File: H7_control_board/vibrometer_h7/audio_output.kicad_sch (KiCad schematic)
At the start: 31 parts, among them J901 PJ-3270, U901 RC4580, U902 TPA6111A2

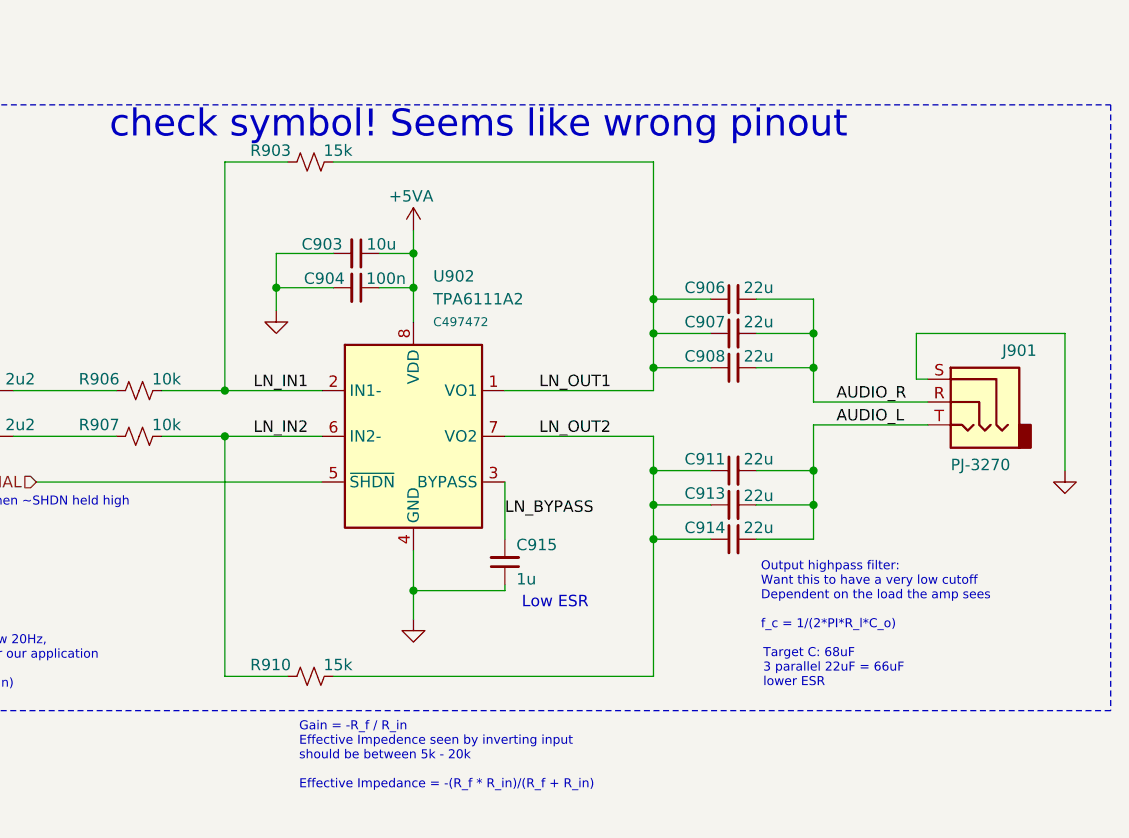
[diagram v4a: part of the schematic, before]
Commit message: cleaned up silkscreen
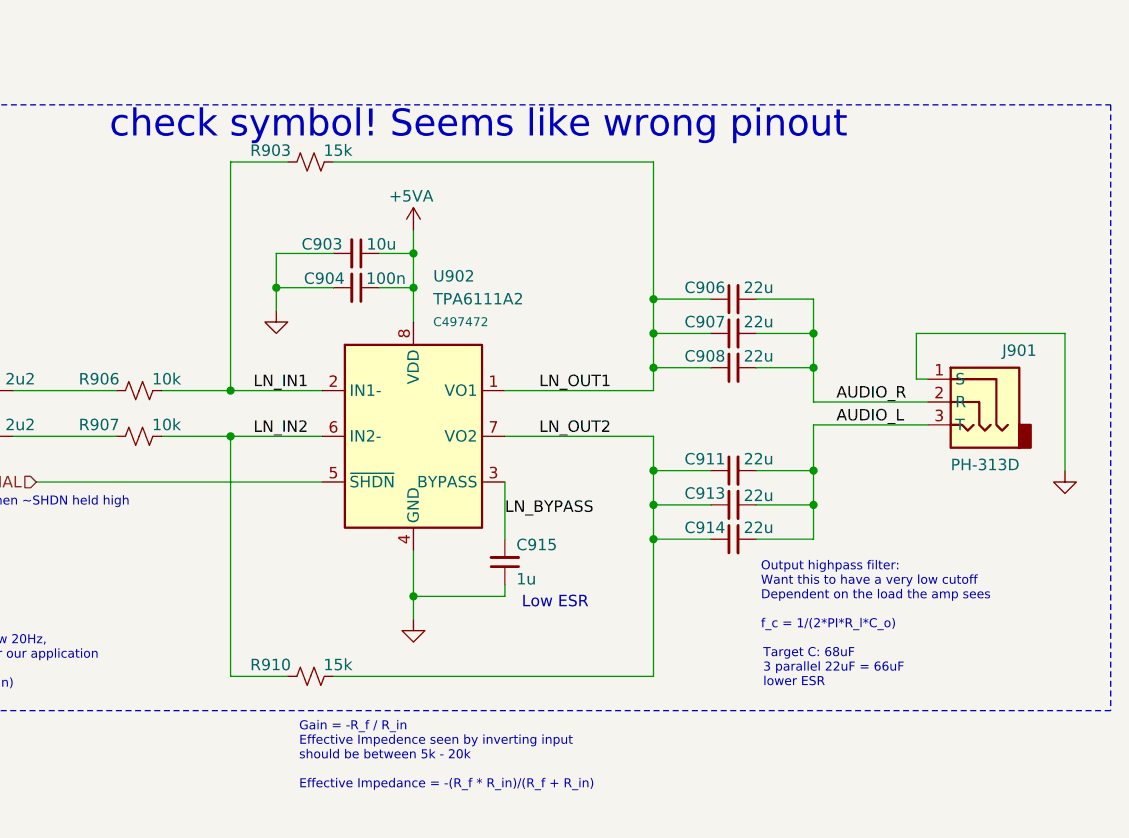
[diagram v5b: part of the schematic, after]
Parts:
- J901: value PJ-3270 -> PH-313D; footprint footprints:AUDIO-TH_PJ-3270 -> footprints:AUDIO-SMD_PJ-313D-2; LCSC C381134 -> C668608
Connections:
- net AUDIO_L: now also J901.3 (T); no longer J901.T
- net AUDIO_R: now also J901.2 (R); no longer J901.R
- net GND: now also J901.1 (S); no longer J901.S
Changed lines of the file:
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@@
 	(paper "A4")
 	(junction
-		(at 193.04 128.905)
-		(diameter 0)
-		(color 0 0 0 0)
-	)
-	(junction
 		(at 219.71 115.57)
 		(diameter 0)
@@
 	)
 	(junction
+		(at 172.72 106.68)
+		(diameter 0)
+		(color 0 0 0 0)
+	)
+	(junction
 		(at 193.04 95.25)
 		(diameter 0)
@@
 	)
 	(junction
-		(at 172.085 111.76)
-		(diameter 0)
-		(color 0 0 0 0)
-	)
-	(junction
 		(at 177.8 95.25)
 		(diameter 0)
@@
 	)
 	(junction
-		(at 172.085 106.68)
-		(diameter 0)
-		(color 0 0 0 0)
-	)
-	(junction
 		(at 66.04 152.4)
 		(diameter 0)
@@
 	)
 	(junction
+		(at 172.72 111.76)
+		(diameter 0)
+		(color 0 0 0 0)
+	)
+	(junction
 		(at 95.25 134.62)
 		(diameter 0)
@@
 	)
 	(junction
+		(at 193.04 129.54)
+		(diameter 0)
+		(color 0 0 0 0)
+	)
+	(junction
 		(at 54.61 132.08)
 		(diameter 0)
@@
 	(wire
 		(pts
-			(xy 172.085 81.28) (xy 179.07 81.28)
+			(xy 172.72 81.28) (xy 179.07 81.28)
 		)
 		(stroke
@@
 	(wire
 		(pts
-			(xy 165.1 111.76) (xy 172.085 111.76)
+			(xy 165.1 111.76) (xy 172.72 111.76)
 		)
 		(stroke
@@
 	(wire
 		(pts
-			(xy 165.1 106.68) (xy 172.085 106.68)
+			(xy 165.1 106.68) (xy 172.72 106.68)
 		)
 		(stroke
@@
 	(wire
 		(pts
-			(xy 193.04 128.905) (xy 203.2 128.905)
+			(xy 193.04 129.54) (xy 203.2 129.54)
+		)
+		(stroke
+			(width 0)
+			(type default)
+		)
+	)
+	(wire
+		(pts
+			(xy 172.72 111.76) (xy 182.88 111.76)
 		)
 		(stroke
@@
 	(wire
 		(pts
-			(xy 193.04 128.905) (xy 193.04 124.46)
+			(xy 193.04 124.46) (xy 193.04 129.54)
 		)
 		(stroke
@@
 	(wire
 		(pts
-			(xy 172.085 81.28) (xy 172.085 106.68)
+			(xy 172.72 81.28) (xy 172.72 106.68)
 		)
 		(stroke
@@
 	(wire
 		(pts
-			(xy 172.085 106.68) (xy 182.88 106.68)
-		)
-		(stroke
-			(width 0)
-			(type default)
-		)
-	)
-	(wire
-		(pts
 			(xy 74.93 69.85) (xy 54.61 69.85)
 		)
@@
 	(wire
 		(pts
+			(xy 172.72 106.68) (xy 182.88 106.68)
+		)
+		(stroke
+			(width 0)
+			(type default)
+		)
+	)
+	(wire
+		(pts
 			(xy 265.43 100.33) (xy 265.43 115.57)
 		)
@@
 	(wire
 		(pts
-			(xy 203.2 128.27) (xy 203.2 128.905)
+			(xy 203.2 128.27) (xy 203.2 129.54)
 		)
 		(stroke
@@
 	(wire
 		(pts
-			(xy 179.07 138.43) (xy 172.085 138.43)
+			(xy 179.07 138.43) (xy 172.72 138.43)
 		)
 		(stroke
@@
 	(wire
 		(pts
-			(xy 193.04 132.08) (xy 193.04 128.905)
+			(xy 193.04 132.08) (xy 193.04 129.54)
 		)
 		(stroke
@@
 	(wire
 		(pts
-			(xy 172.085 138.43) (xy 172.085 111.76)
+			(xy 172.72 138.43) (xy 172.72 111.76)
 		)
 		(stroke
@@
 		(pts
 			(xy 74.93 137.16) (xy 74.93 142.24)
-		)
-		(stroke
-			(width 0)
-			(type default)
-		)
-	)
-	(wire
-		(pts
-			(xy 172.085 111.76) (xy 182.88 111.76)
 		)
 		(stroke
@@
 			)
 		)
-		(property "Value" "PJ-3270"
+		(property "Value" "PH-313D"
 			(at 252.73 114.935 0)
 			(effects
@@
 			)
 		)
-		(property "Footprint" "footprints:AUDIO-TH_PJ-3270"
-			(at 255.27 107.95 0)
-			(effects
-				(font
-					(size 1.27 1.27)
-				)
-				(hide yes)
-			)
-		)
-		(property "Datasheet" "https://wmsc.lcsc.com/wmsc/upload/file/pdf/v2/lcsc/2110151630_XKB-Connection-PJ-3270_C381134.pdf"
-			(at 255.27 107.95 0)
+		(property "Footprint" "footprints:AUDIO-SMD_PJ-313D-2"
+			(at 255.27 95.758 0)
+			(effects
+				(font
+					(size 1.27 1.27)
+				)
+				(hide yes)
+			)
+		)
+		(property "Datasheet" "https://www.lcsc.com/datasheet/lcsc_datasheet_2006181822_SHOU-HAN-PJ-313D_C668608.pdf"
+			(at 255.27 97.79 0)
 			(effects
 				(font
@@
 		)
 		(property "Description" "Audio Jack, 3 Poles (Stereo / TRS)"
-			(at 255.27 107.95 0)
-			(effects
-				(font
-					(size 1.27 1.27)
-				)
-				(hide yes)
-			)
-		)
-		(property "LCSC" "C381134"
-			(at 255.27 107.95 0)
-			(effects
-				(font
-					(size 1.27 1.27)
-				)
-				(hide yes)
-			)
-		)
-		(pin "T"
-		)
-		(pin "R"
-		)
-		(pin "S"
+			(at 255.27 100.076 0)
+			(effects
+				(font
+					(size 1.27 1.27)
+				)
+				(hide yes)
+			)
+		)
+		(property "LCSC" "C668608"
+			(at 255.27 102.108 0)
+			(effects
+				(font
+					(size 1.27 1.27)
+				)
+				(hide yes)
+			)
+		)
+		(pin "2"
+		)
+		(pin "1"
+		)
+		(pin "3"
 		)
 		(instances

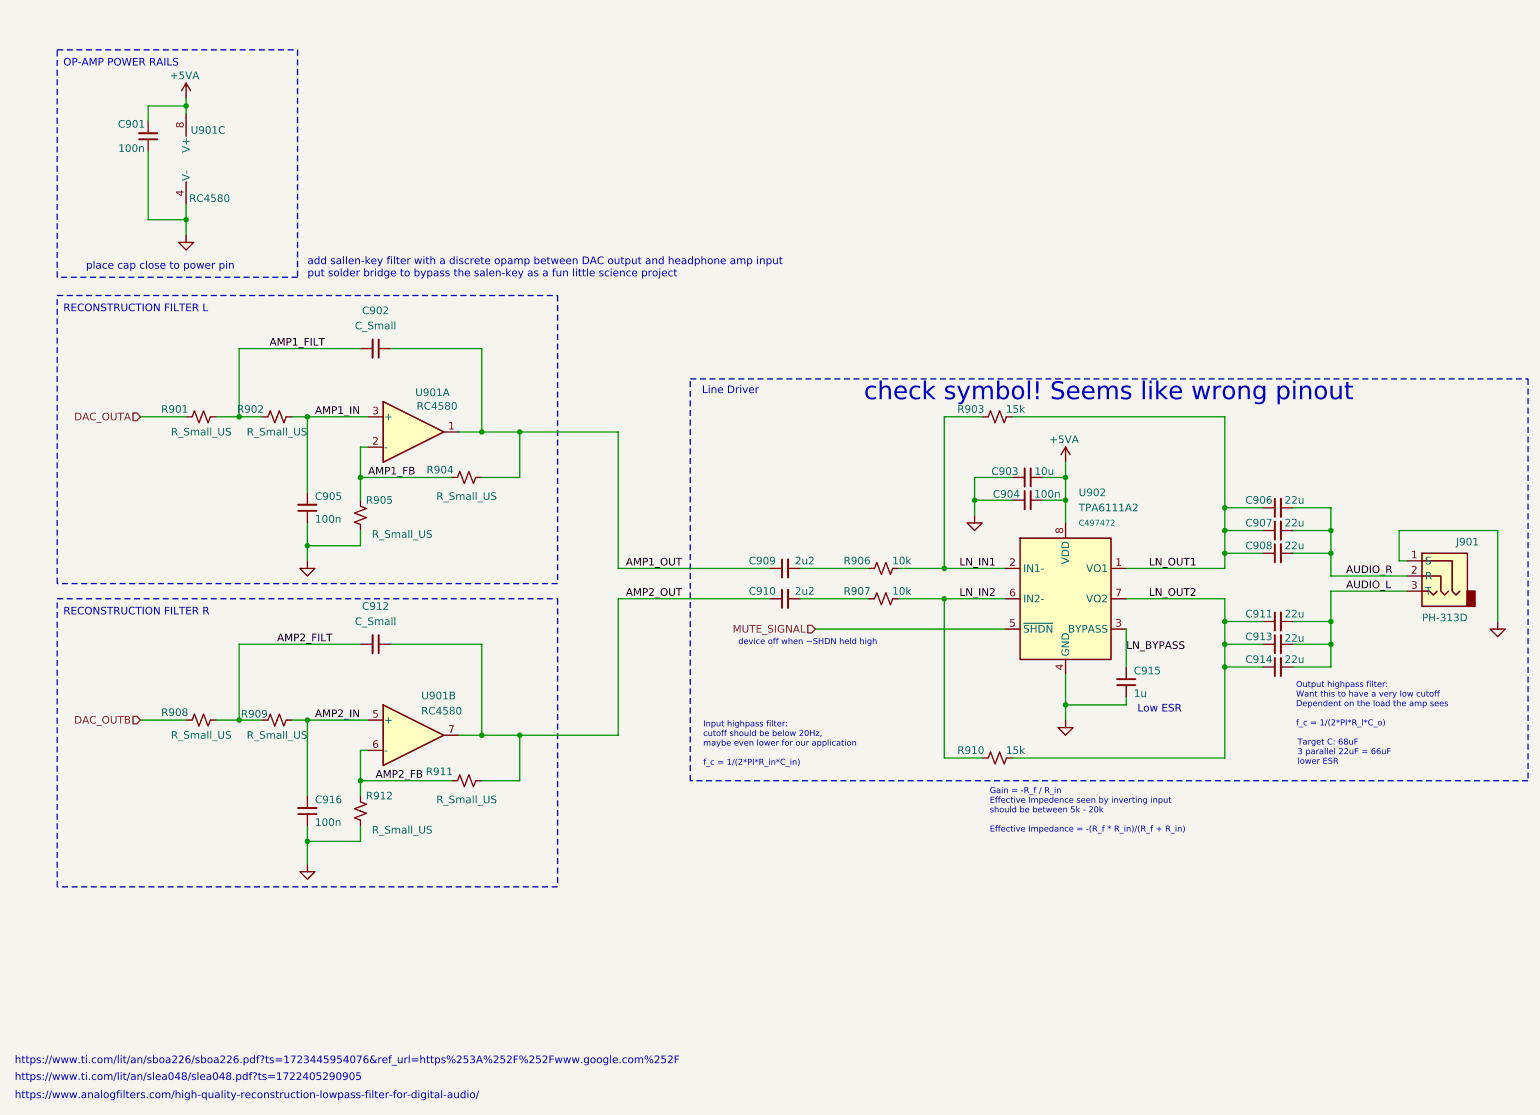
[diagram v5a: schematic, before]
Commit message: added indicator leds
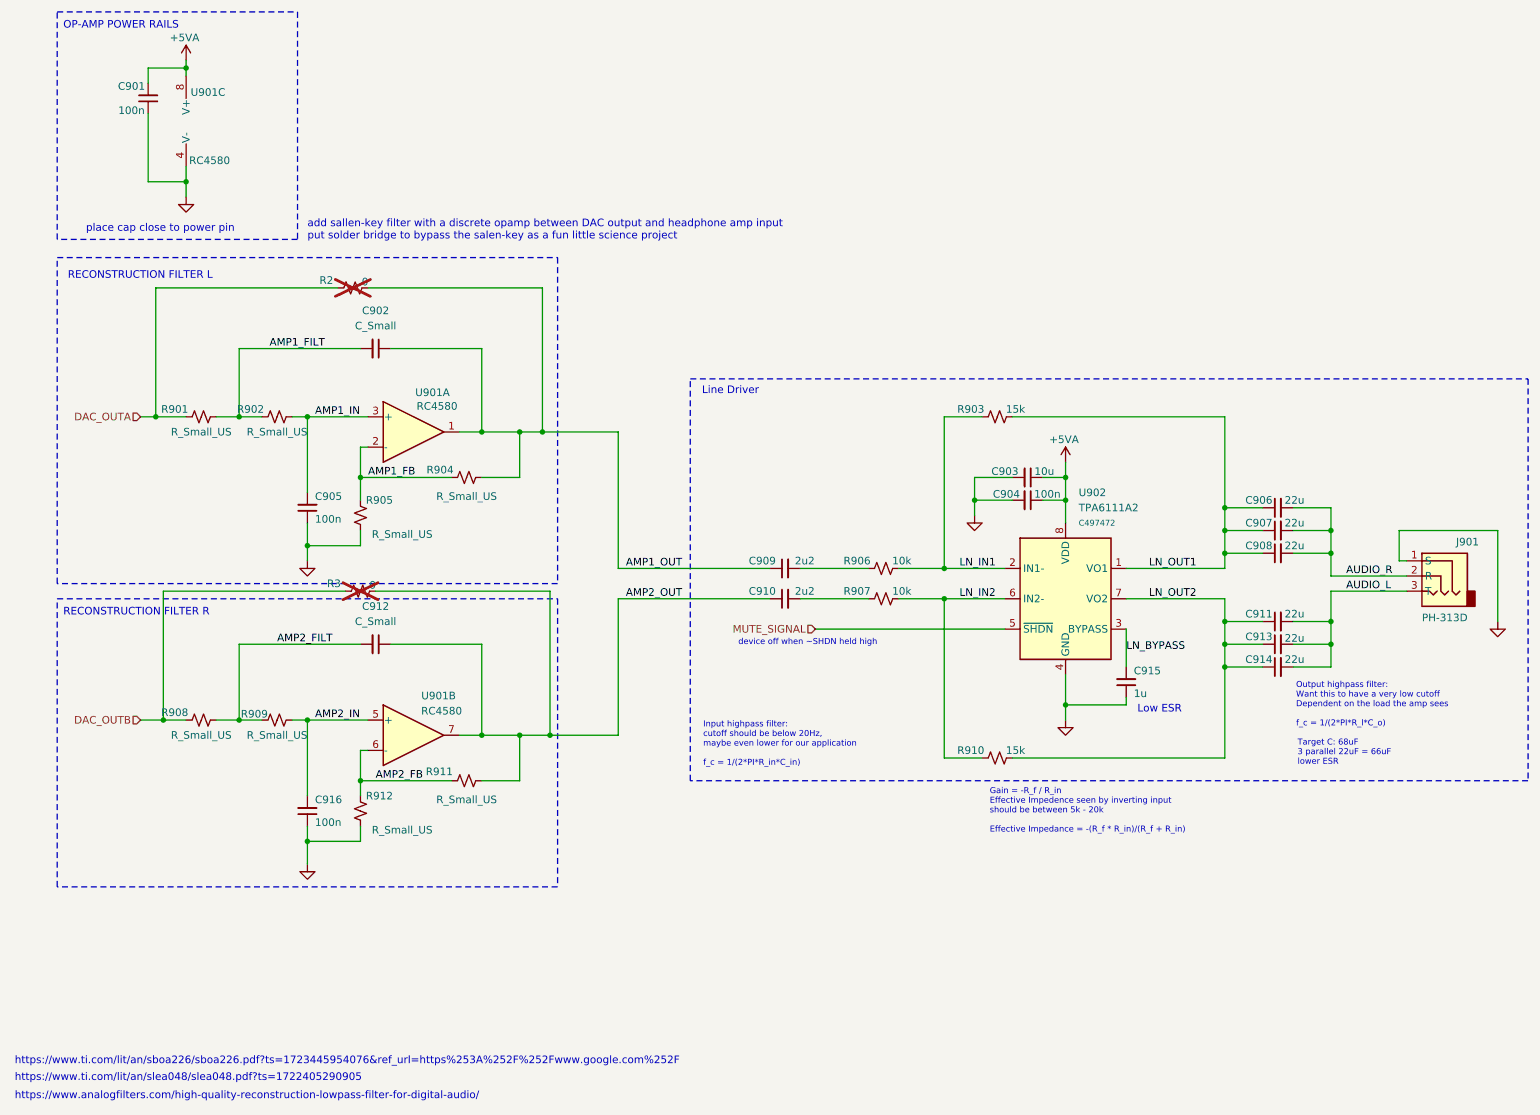
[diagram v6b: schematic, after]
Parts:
- added R2, R3: 0, Resistor_SMD:R_0603_1608Metric, symbol Device:R_Small_US
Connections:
- net AMP1_OUT: now also R2.2
- net AMP2_OUT: now also R3.2
- net DAC_OUTA: now also R2.1
- net DAC_OUTB: now also R3.1
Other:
- note removed: "check symbol! Seems like wrong pinout"
- moved on the sheet: C901, U901C

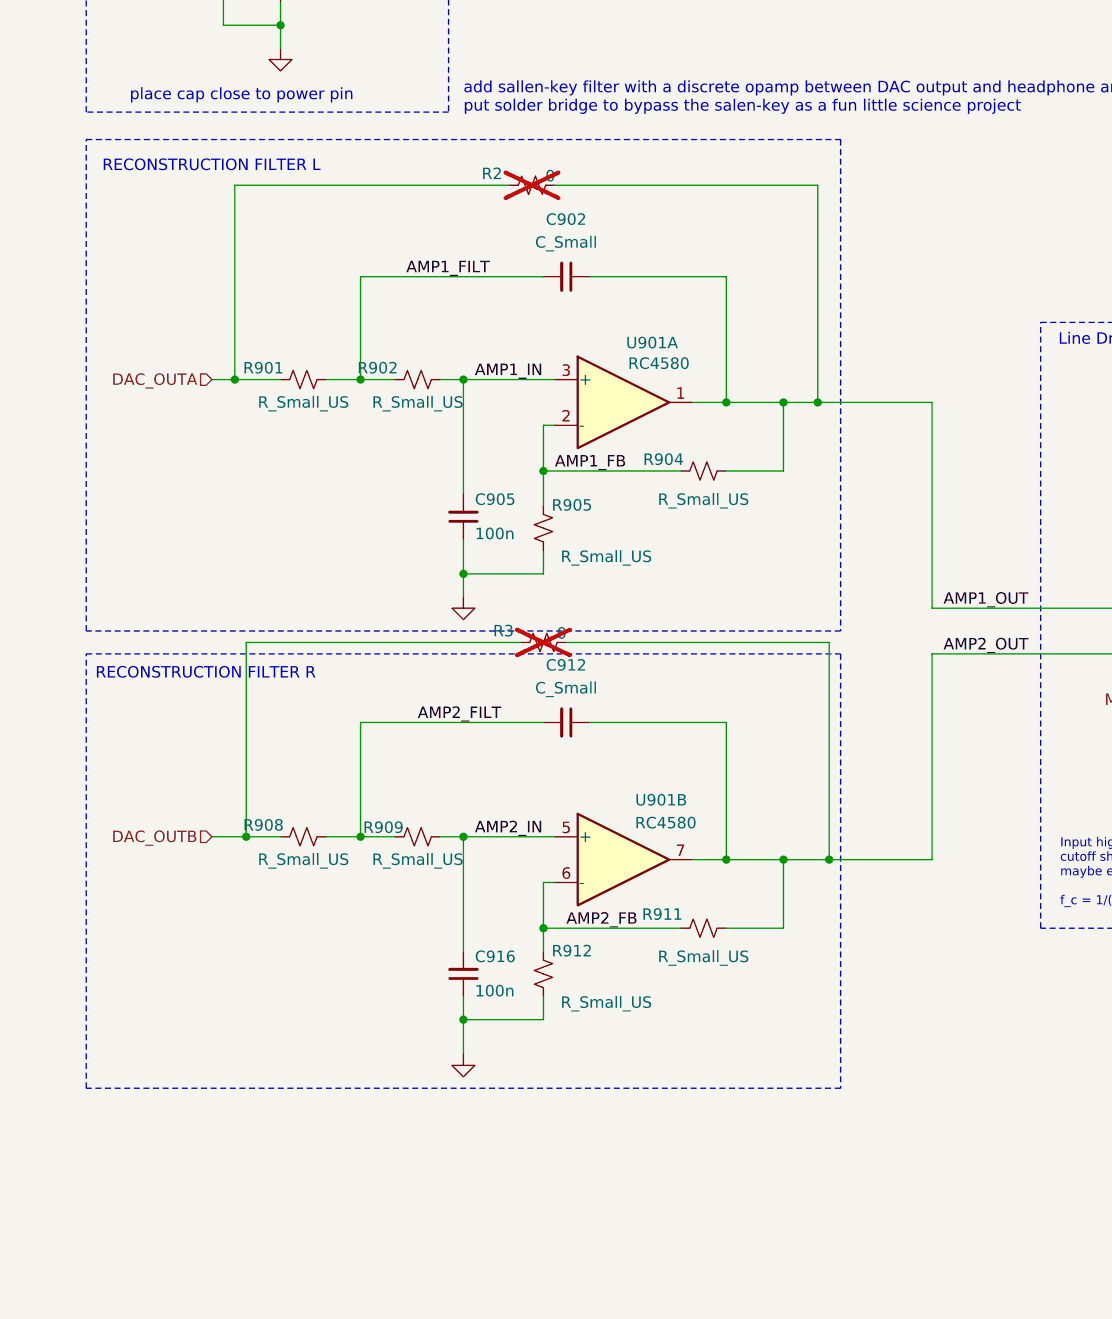
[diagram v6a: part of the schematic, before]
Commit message: connectors, they are so BIG whyyyy john, whyyy
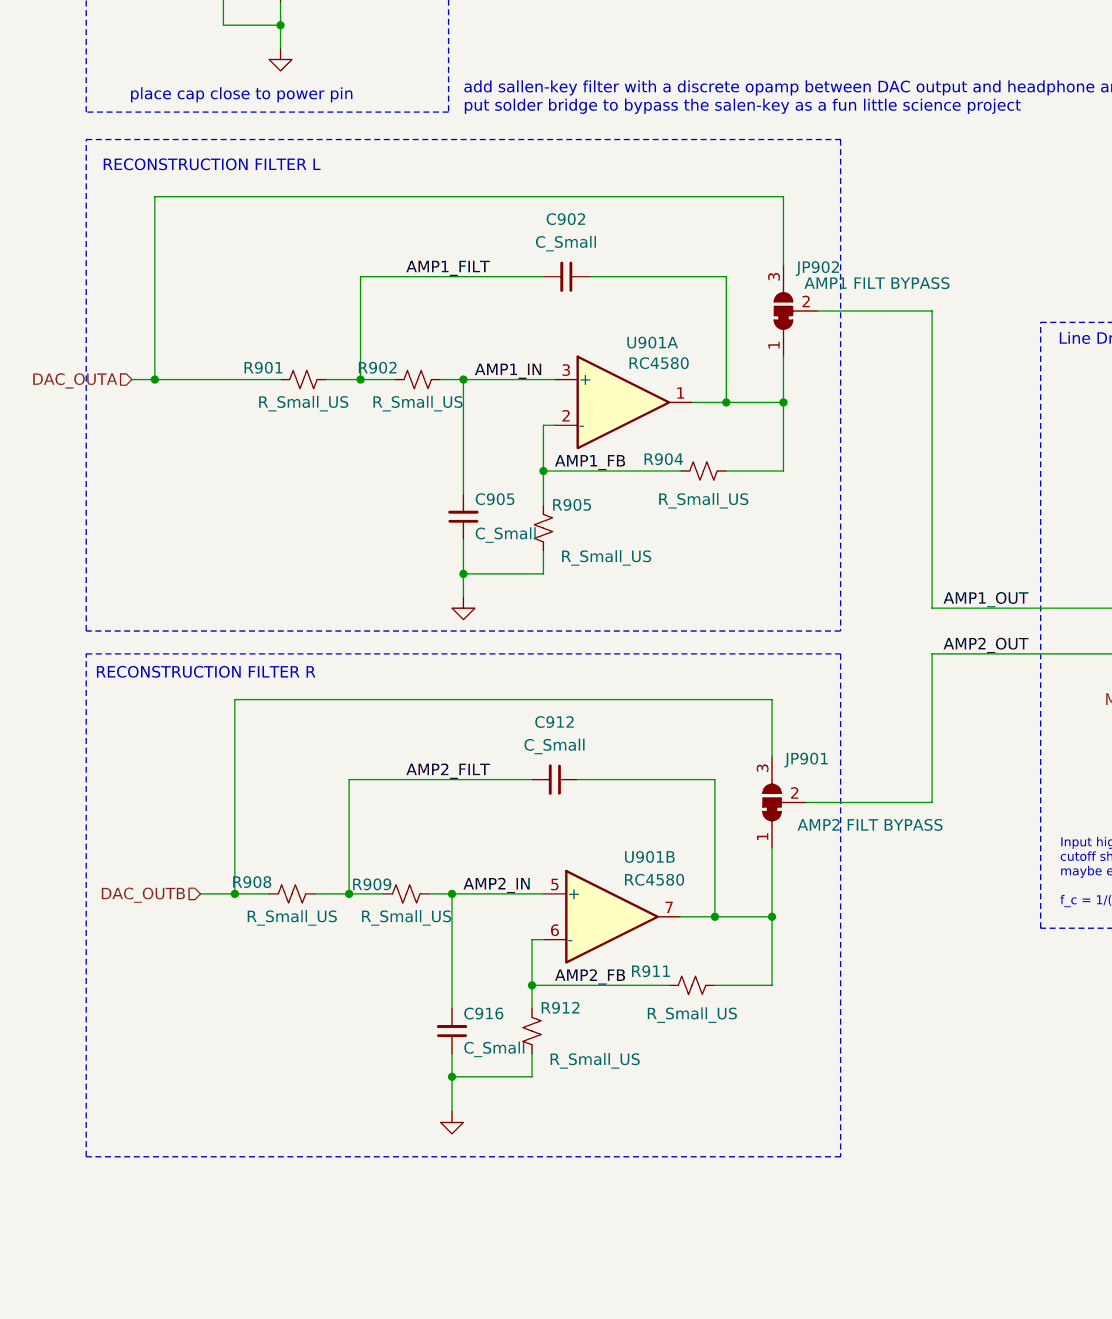
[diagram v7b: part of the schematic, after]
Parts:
- removed R2, R3: 0, Resistor_SMD:R_0603_1608Metric, symbol Device:R_Small_US
- added JP901: AMP2 FILT BYPASS, Jumper:SolderJumper-3_P1.3mm_Bridged12_RoundedPad1.0x1.5mm, symbol Jumper:SolderJumper_3_Bridged12
- added JP902: AMP1 FILT BYPASS, Jumper:SolderJumper-3_P1.3mm_Bridged12_RoundedPad1.0x1.5mm, symbol Jumper:SolderJumper_3_Bridged12
- C905, C916: value 100n -> C_Small
- R906, R907: footprint Resistor_SMD:R_0603_1608Metric -> Resistor_SMD:R_0402_1005Metric
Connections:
- net AMP1_OUT: now also JP902.2 (C); no longer C902.1, R904.2, U901.1
- net AMP2_OUT: now also JP901.2 (C); no longer C912.1, R911.2, U901.7
- net DAC_OUTA: now also JP902.3 (B)
- net DAC_OUTB: now also JP901.3 (B)
- new net: C902.1, JP902.1 (A), R904.2, U901.1
- new net: C912.1, JP901.1 (A), R911.2, U901.7
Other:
- moved on the sheet: C912, C916, R908, R909, R911, R912, U901B
